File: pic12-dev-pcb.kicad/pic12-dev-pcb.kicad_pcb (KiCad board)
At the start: 2 copper layers, 25.4 x 40.1 mm, 12 parts, among them J1 PGM-Conn, J2 App-Conn1, J3 App-Conn2, J4 Conn_SR, J6 Conn_BB1, U1 PIC12F675-ISN

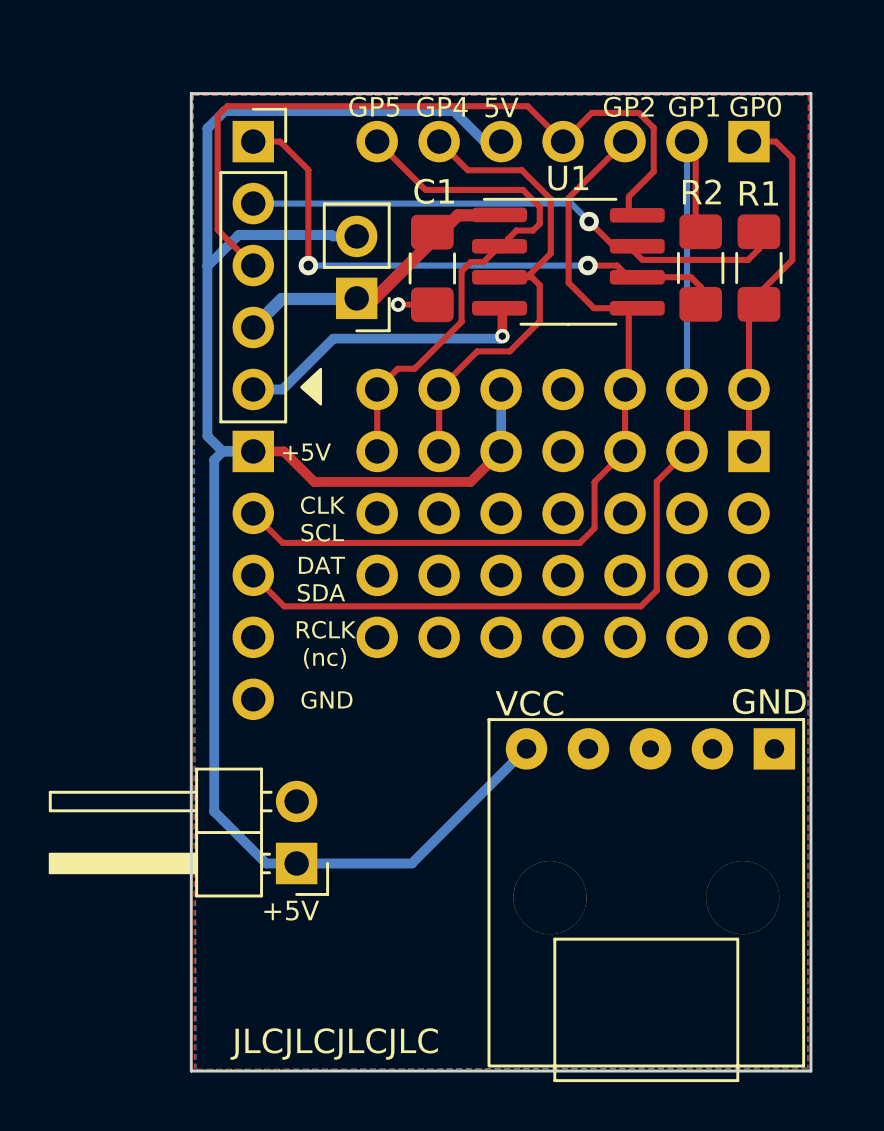
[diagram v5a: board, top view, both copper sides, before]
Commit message: move SR-connector to edge
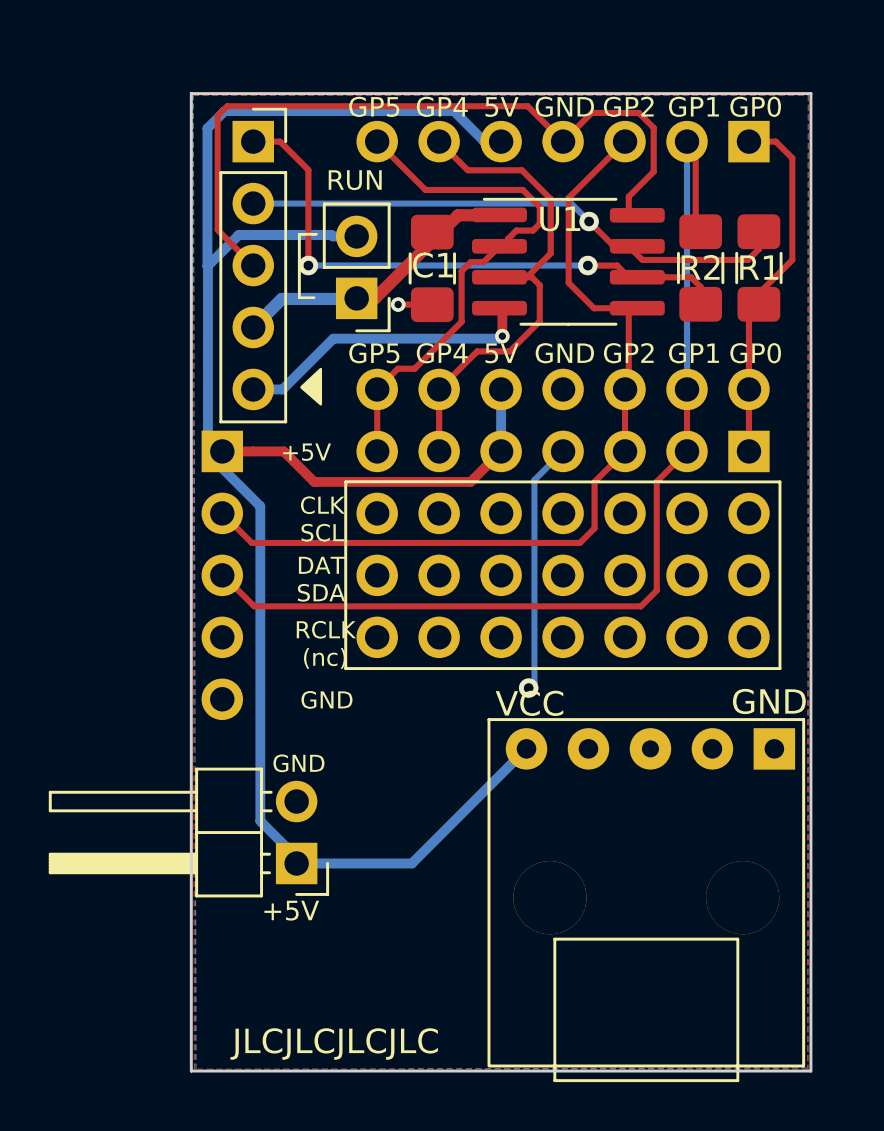
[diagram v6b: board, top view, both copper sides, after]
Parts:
- moved J4 1.27 mm to (97.8, 88.9)
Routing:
- net GND: track 31.5 -> 41.8 mm, vias 1 -> 2
- net /GP1: track 40.1 -> 41.4 mm
- net /GP2: track 34.0 -> 35.3 mm
- net /+5V: track 80.0 -> 79.2 mm
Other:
- board text added: "RUN"

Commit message: optimized labels
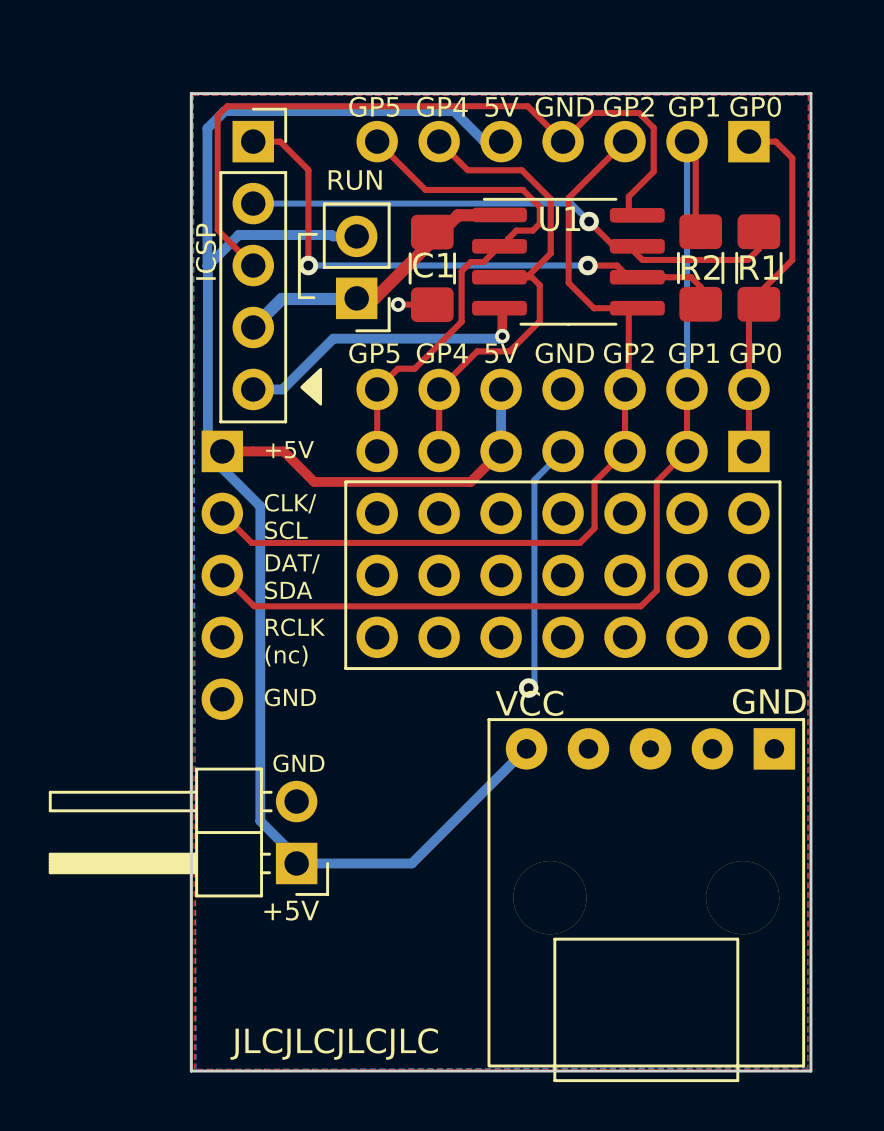
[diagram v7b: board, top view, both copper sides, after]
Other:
- board text added: "CLK/ SCL"
- board text added: "DAT/ SDA"
- board text added: "ICSP"
- board text removed: "CLK SCL"
- board text removed: "DAT SDA"
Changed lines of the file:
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@@
   (general
     (thickness 1.6)
-    (drawings 51)
+    (drawings 52)
     (tracks 144)
     (zones 0)
@@
     )
   )
+  (gr_text ICSP (at 97.15 80.75 90) (layer F.SilkS)
+    (effects (font (size 0.8 0.8) (thickness 0.15)))
+  )
   (gr_line (start 102.85 97.8) (end 102.85 90.15) (layer F.SilkS) (width 0.12))
   (gr_line (start 120.65 97.8) (end 102.85 97.8) (layer F.SilkS) (width 0.12))
@@
     (effects (font (size 0.8 0.8) (thickness 0.15)))
   )
-  (gr_text "RCLK\n(nc)" (at 102 96.7994) (layer F.SilkS)
-    (effects (font (size 0.7 0.7) (thickness 0.15)))
+  (gr_text "RCLK\n(nc)" (at 99.4826 96.6994) (layer F.SilkS)
+    (effects (font (size 0.7 0.7) (thickness 0.15)) (justify left))
   )
   (gr_poly (pts (xy 101.8286 86.9696) (xy 101.0412 86.2838) (xy 101.0412 86.2584) (xy 101.8286 85.5218)) (layer F.SilkS) (width 0.1))
@@
   (gr_line (start 96.57 103.24) (end 121.92 103.24) (layer F.Fab) (width 0.12))
   (gr_line (start 96.57 109.24) (end 121.92 109.24) (layer F.Fab) (width 0.12))
-  (gr_text GND (at 102.0826 99.1108) (layer F.SilkS)
-    (effects (font (size 0.7 0.7) (thickness 0.15)))
-  )
-  (gr_text +5V (at 101.219 88.9508) (layer F.SilkS)
-    (effects (font (size 0.7 0.7) (thickness 0.15)))
-  )
-  (gr_text "CLK\nSCL" (at 101.8794 91.694) (layer F.SilkS)
-    (effects (font (size 0.7 0.7) (thickness 0.15)))
-  )
-  (gr_text "DAT\nSDA" (at 101.8286 94.1578) (layer F.SilkS)
-    (effects (font (size 0.7 0.7) (thickness 0.15)))
+  (gr_text GND (at 99.4826 99.0108) (layer F.SilkS)
+    (effects (font (size 0.7 0.7) (thickness 0.15)) (justify left))
+  )
+  (gr_text +5V (at 99.4826 88.8508) (layer F.SilkS)
+    (effects (font (size 0.7 0.7) (thickness 0.15)) (justify left))
+  )
+  (gr_text "CLK/\nSCL" (at 99.4826 91.594) (layer F.SilkS)
+    (effects (font (size 0.7 0.7) (thickness 0.15)) (justify left))
+  )
+  (gr_text "DAT/\nSDA" (at 99.4826 94.0578) (layer F.SilkS)
+    (effects (font (size 0.7 0.7) (thickness 0.15)) (justify left))
   )
   (gr_text "Rev 3" (at 99.695 112.9284) (layer B.SilkS)

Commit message: Rev4: fixed order of pins of SR-connector
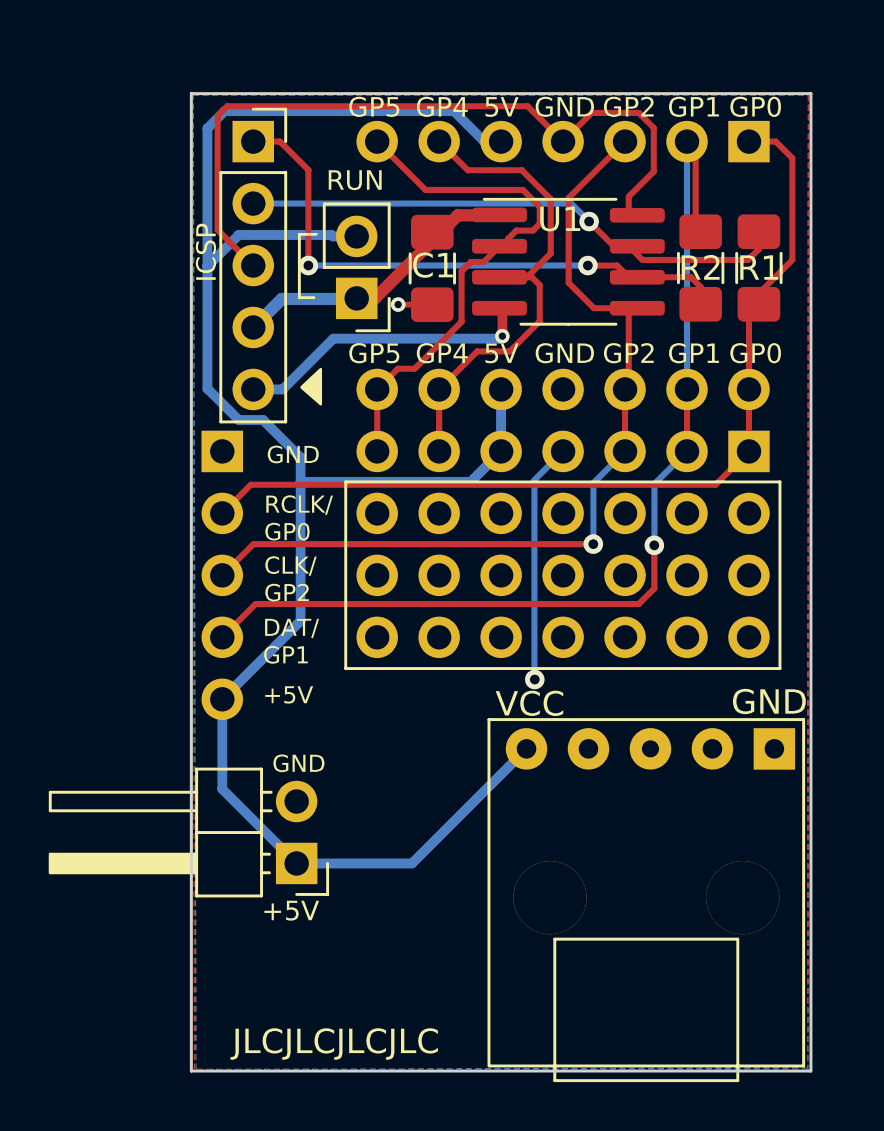
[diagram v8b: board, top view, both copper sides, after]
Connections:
- J4 pad 1: /+5V -> GND
- J4 pad 2: /GP2 -> /GP0
- J4 pad 3: /GP1 -> /GP2
- J4 pad 4: /RCLK -> /GP1
- J4 pad 5: GND -> /+5V
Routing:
- net /GP0: track 15.1 -> 37.7 mm
- net /+5V: track 79.2 -> 77.6 mm
- net /GP2: track 35.3 -> 35.7 mm, vias 0 -> 1
- net /GP1: track 41.4 -> 41.3 mm, vias 0 -> 1
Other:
- board text added: "CLK/ GP2"
- board text added: "DAT/ GP1"
- board text added: "RCLK/ GP0"
- board text added: "Rev 4"
- board text removed: "CLK/ SCL"
- board text removed: "DAT/ SDA"
- board text removed: "RCLK (nc)"
- board text removed: "Rev 3"
